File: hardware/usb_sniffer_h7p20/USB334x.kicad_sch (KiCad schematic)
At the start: 16 parts, among them J2 USB_C_Receptacle_USB2.0_16P, J3 USB_A, U10 CH132C, U2 LM2903A-VR, U3 LM2903A-VR, U4 LM2903A-VR

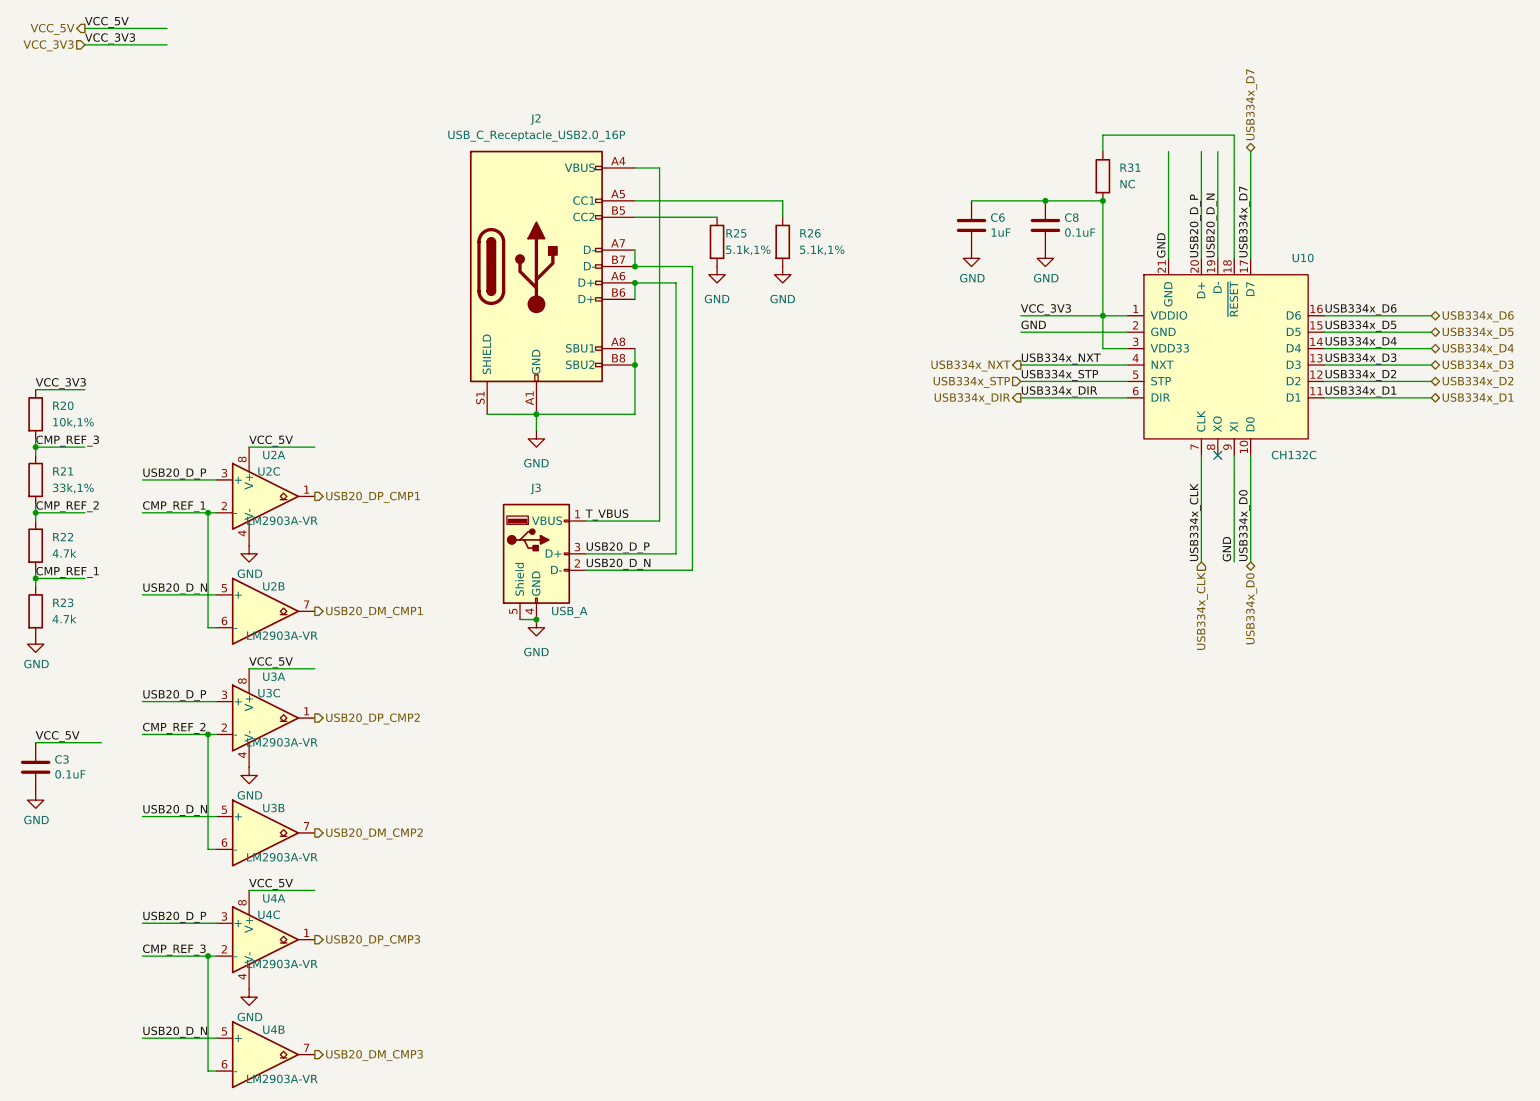
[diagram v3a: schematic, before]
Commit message: [usb_sniffer_h7p20] CH132C测试无数据，回退USB3343
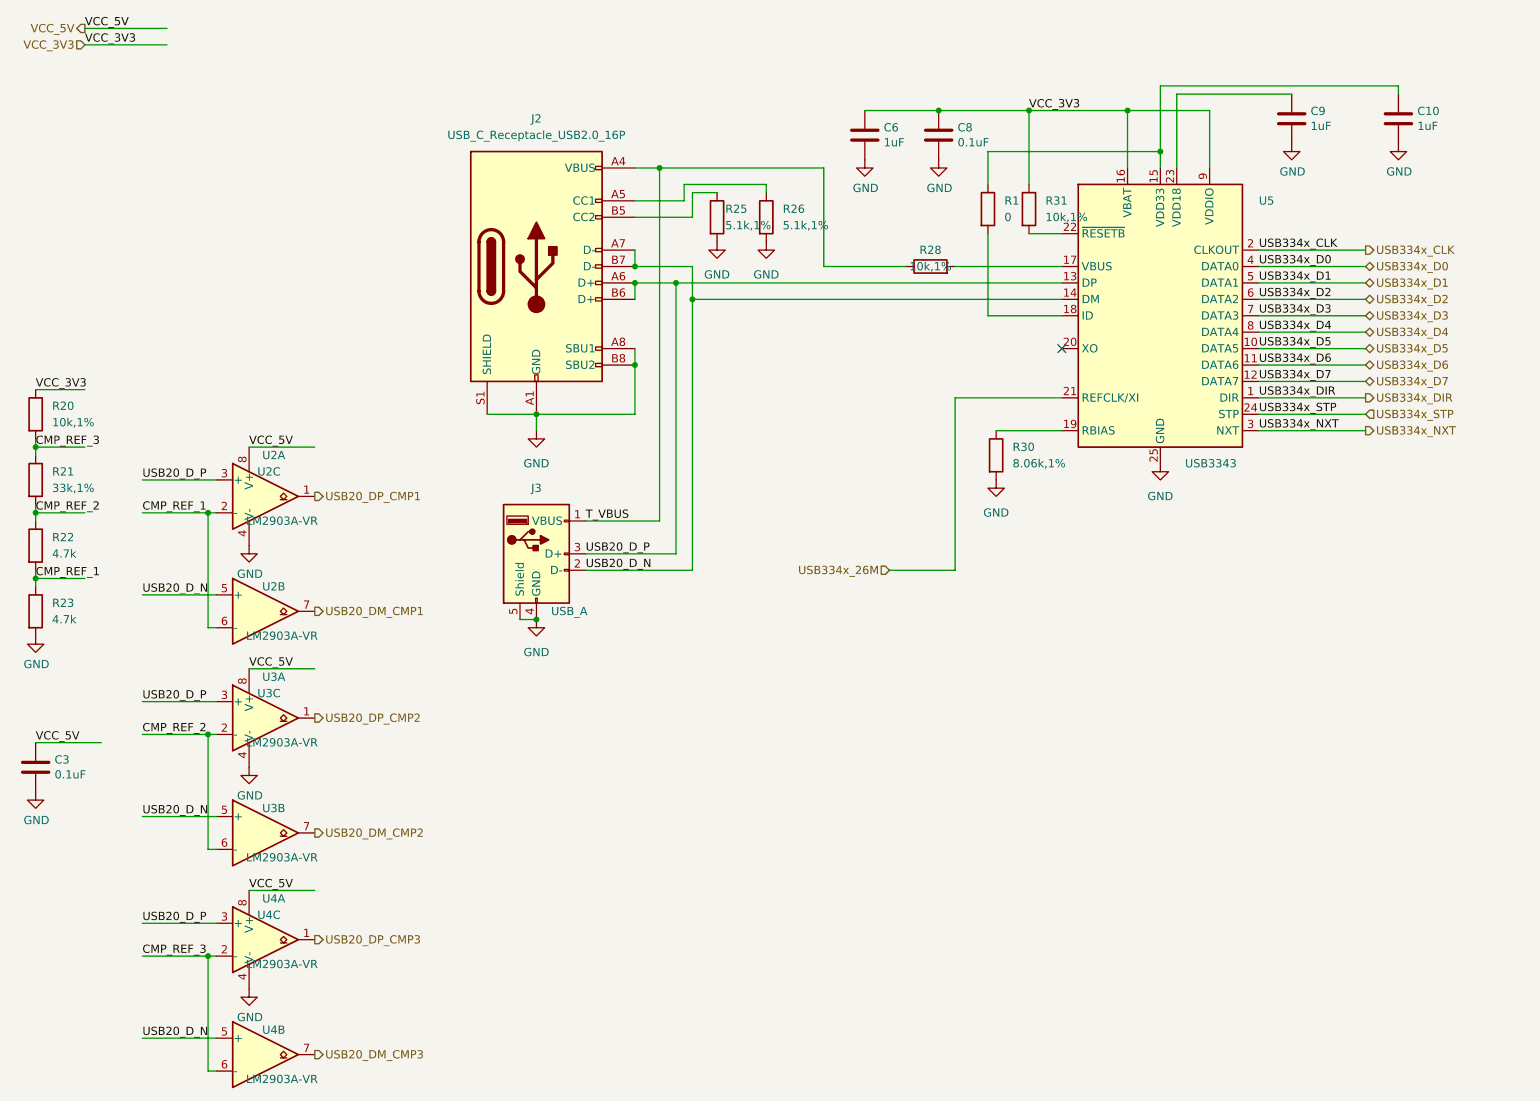
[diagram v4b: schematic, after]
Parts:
- removed U10: CH132C, vllogic:QFN20C_2x2, symbol vllogic_chip:CH132C
- added C10, C9: 1uF, Capacitor_SMD:C_0402_1005Metric, symbol Device:C
- added R1: 0, Resistor_SMD:R_0402_1005Metric, symbol Device:R
- added R28: 10k,1%, Resistor_SMD:R_0402_1005Metric, symbol Device:R
- added R30: 8.06k,1%, Resistor_SMD:R_0402_1005Metric, symbol Device:R
- added U5: USB3343, vllogic:QFN-24-1EP_4x4mm_P0.5mm_EP2.6x2.6mm, symbol Interface_USB:USB3343
- R31: value NC -> 10k,1%
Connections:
- net GND: now also C10.1, C9.1, R30.2, U5.25 (GND)
- net T_VBUS: now also R28.1
- net USB20_D_N: now also U5.14 (DM)
- net USB20_D_P: now also U5.13 (DP)
- net USB334x_CLK: now also U5.2 (CLKOUT)
- net USB334x_D0: now also U5.4 (DATA0)
- net USB334x_D1: now also U5.5 (DATA1)
- net USB334x_D2: now also U5.6 (DATA2)
- net USB334x_D3: now also U5.7 (DATA3)
- net USB334x_D4: now also U5.8 (DATA4)
- net USB334x_D5: now also U5.10 (DATA5)
- net USB334x_D6: now also U5.11 (DATA6)
- net USB334x_D7: now also U5.12 (DATA7)
- net USB334x_DIR: now also U5.1 (DIR)
- net USB334x_NXT: now also U5.3 (NXT)
- net USB334x_STP: now also U5.24 (STP)
- net VCC_3V3: now also R31.1, U5.16 (VBAT), U5.9 (VDDIO); no longer R31.2
- new net: R31.2, U5.22 (~{RESETB})
- new net: R30.1, U5.19 (RBIAS)
- new net: C10.2, R1.1, U5.15 (VDD33)
- new net: R28.2, U5.17 (VBUS)
- new net: R1.2, U5.18 (ID)
- new net: C9.2, U5.23 (VDD18)
- new net USB334x_26M: U5.21 (REFCLK/XI)
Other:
- moved on the sheet: C6, C8, R25, R26, R31

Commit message: [usb_sniffer_h7p20] 换GSV332-MR，待测试
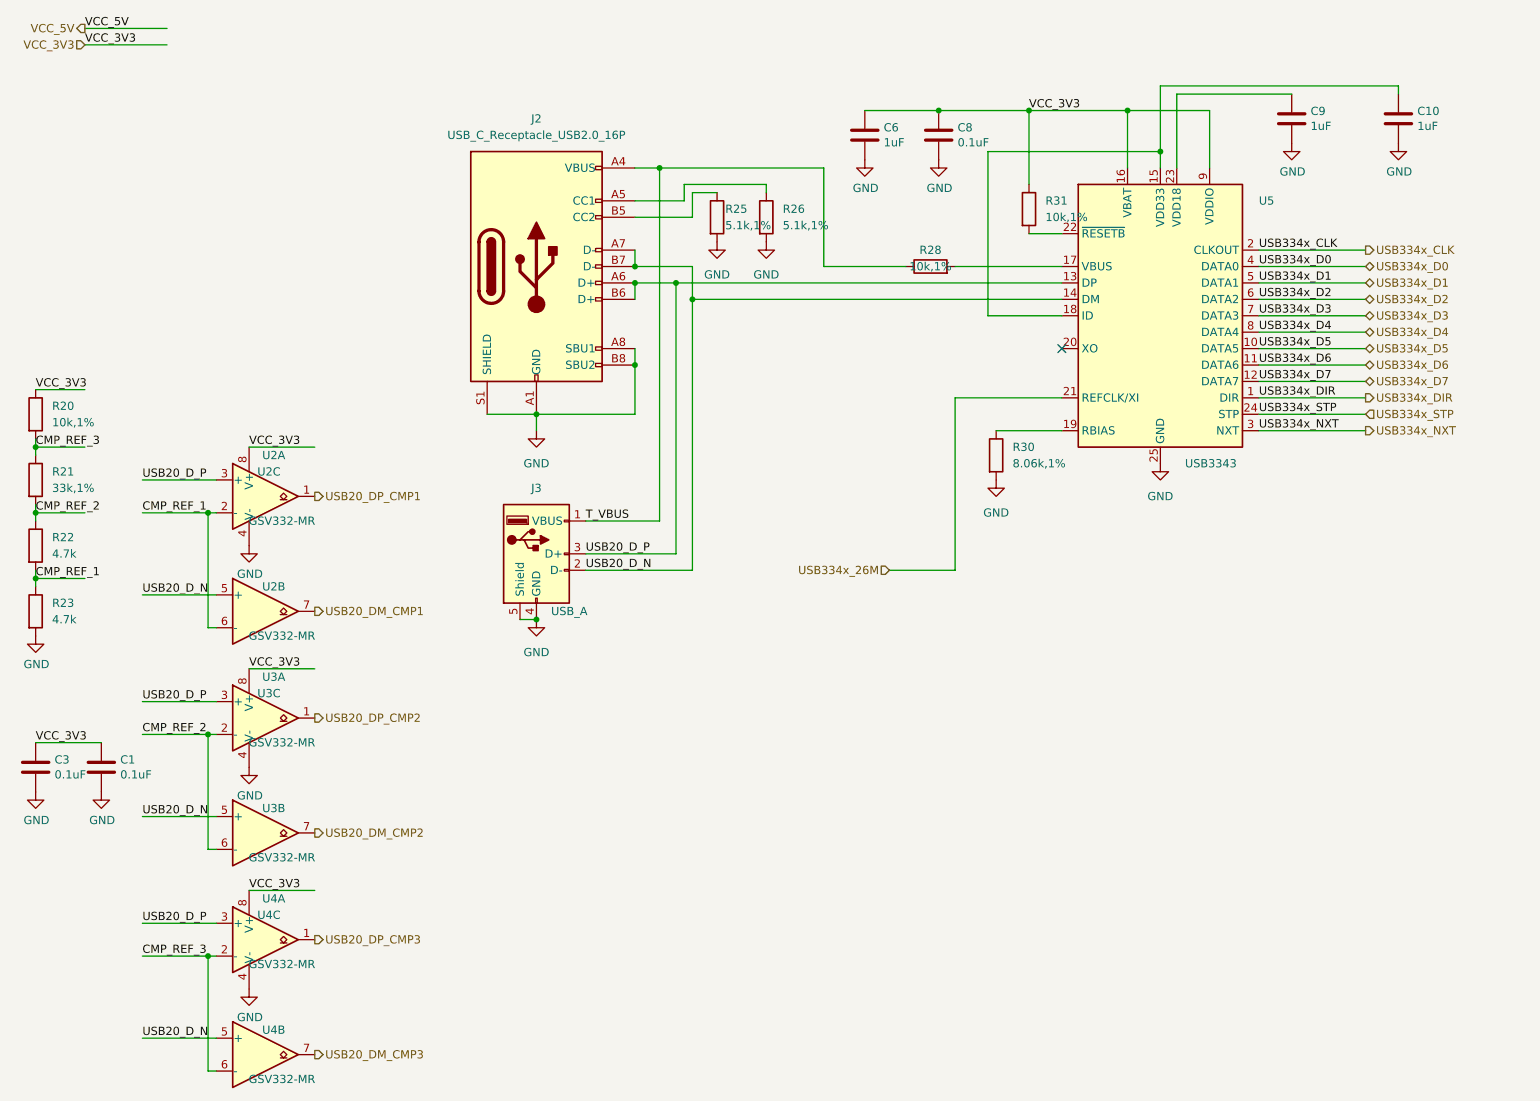
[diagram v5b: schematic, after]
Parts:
- removed R1: 0, Resistor_SMD:R_0402_1005Metric, symbol Device:R
- added C1: 0.1uF, Capacitor_SMD:C_0402_1005Metric, symbol Device:C
- U2, U3, U4: value LM2903A-VR -> GSV332-MR
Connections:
- net GND: now also C1.1
- net VCC_3V3: now also C3.2, U2.8 (V+), U3.8 (V+), U4.8 (V+), C1.2
- net VCC_5V: no longer C3.2, U2.8 (V+), U3.8 (V+), U4.8 (V+)
- net at C10.2, U5.15 (VDD33): now also U5.18 (ID)
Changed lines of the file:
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@@
 	(wire
 		(pts
-			(xy 171.45 50.8) (xy 171.45 55.88)
-		)
-		(stroke
-			(width 0)
-			(type default)
-		)
-	)
-	(wire
-		(pts
 			(xy 213.36 81.28) (xy 229.87 81.28)
 		)
@@
 	(wire
 		(pts
-			(xy 171.45 63.5) (xy 171.45 76.2)
+			(xy 171.45 50.8) (xy 171.45 76.2)
 		)
 		(stroke
@@
 		)
 	)
-	(label "VCC_5V"
-		(at 57.15 130.81 0)
+	(label "VCC_3V3"
+		(at 24.13 87.63 0)
 		(effects
 			(font
@@
 		)
 	)
-	(label "VCC_3V3"
-		(at 24.13 87.63 0)
+	(label "USB334x_NXT"
+		(at 213.36 93.98 0)
 		(effects
 			(font
@@
 		)
 	)
-	(label "USB334x_NXT"
-		(at 213.36 93.98 0)
+	(label "VCC_3V3"
+		(at 24.13 142.24 0)
 		(effects
 			(font
@@
 		)
 	)
-	(label "VCC_5V"
-		(at 57.15 96.52 0)
-		(effects
-			(font
-				(size 1.27 1.27)
-			)
-			(justify left bottom)
-		)
-	)
-	(label "VCC_5V"
-		(at 57.15 165.1 0)
-		(effects
-			(font
-				(size 1.27 1.27)
-			)
-			(justify left bottom)
-		)
-	)
 	(label "CMP_REF_3"
 		(at 40.64 175.26 0)
@@
 		)
 	)
-	(label "VCC_5V"
-		(at 24.13 142.24 0)
+	(label "USB334x_D4"
+		(at 213.36 78.74 0)
 		(effects
 			(font
@@
 		)
 	)
-	(label "USB334x_D4"
-		(at 213.36 78.74 0)
+	(label "CMP_REF_3"
+		(at 24.13 96.52 0)
 		(effects
 			(font
@@
 		)
 	)
-	(label "CMP_REF_3"
-		(at 24.13 96.52 0)
+	(label "VCC_3V3"
+		(at 57.15 165.1 0)
 		(effects
 			(font
@@
 		)
 	)
+	(label "VCC_3V3"
+		(at 57.15 130.81 0)
+		(effects
+			(font
+				(size 1.27 1.27)
+			)
+			(justify left bottom)
+		)
+	)
 	(label "USB334x_D6"
 		(at 213.36 83.82 0)
@@
 		)
 	)
+	(label "VCC_3V3"
+		(at 57.15 96.52 0)
+		(effects
+			(font
+				(size 1.27 1.27)
+			)
+			(justify left bottom)
+		)
+	)
 	(label "USB334x_D3"
 		(at 213.36 76.2 0)
@@
 			)
 		)
-		(property "Value" "LM2903A-VR"
+		(property "Value" "GSV332-MR"
 			(at 58.42 142.24 0)
 			(effects
@@
 			)
 		)
-		(property "Value" "LM2903A-VR"
+		(property "Value" "GSV332-MR"
 			(at 62.23 142.24 0)
 			(effects
@@
 			)
 		)
-		(property "Value" "LM2903A-VR"
+		(property "Value" "GSV332-MR"
 			(at 62.23 160.02 0)
 			(effects
@@
 	)
 	(symbol
+		(lib_id "power:GND")
+		(at 34.29 149.86 0)
+		(unit 1)
+		(exclude_from_sim no)
+		(in_bom yes)
+		(on_board yes)
+		(dnp no)
+		(property "Reference" "#PWR01"
+			(at 34.29 156.21 0)
+			(effects
+				(font
+					(size 1.27 1.27)
+				)
+				(hide yes)
+			)
+		)
+		(property "Value" "GND"
+			(at 34.417 154.2542 0)
+			(effects
+				(font
+					(size 1.27 1.27)
+				)
+			)
+		)
+		(property "Footprint" ""
+			(at 34.29 149.86 0)
+			(effects
+				(font
+					(size 1.27 1.27)
+				)
+				(hide yes)
+			)
+		)
+		(property "Datasheet" ""
+			(at 34.29 149.86 0)
+			(effects
+				(font
+					(size 1.27 1.27)
+				)
+				(hide yes)
+			)
+		)
+		(property "Description" ""
+			(at 34.29 149.86 0)
+			(effects
+				(font
+					(size 1.27 1.27)
+				)
+			)
+		)
+		(pin "1"
+		)
+		(instances
+			(project "usb_sniffer_h7p20"
+				(path "/5a8287a8-9f7a-4e60-a3bf-19c1227b20fe/f5b7f82e-a1df-40b6-9f59-134d2c724739"
+					(reference "#PWR01")
+					(unit 1)
+				)
+			)
+		)
+	)
+	(symbol
 		(lib_id "Connector:USB_A")
 		(at 101.6 113.03 0)
@@
 			)
 		)
-		(property "Datasheet" " ~"
+		(property "Datasheet" "~"
 			(at 105.41 114.3 0)
 			(effects
@@
 			)
 		)
-		(property "Value" "LM2903A-VR"
+		(property "Value" "GSV332-MR"
 			(at 62.23 107.95 0)
 			(effects
@@
 			)
 		)
-		(property "Value" "LM2903A-VR"
+		(property "Value" "GSV332-MR"
 			(at 62.23 125.73 0)
 			(effects
@@
 	)
 	(symbol
+		(lib_id "Device:C")
+		(at 34.29 146.05 180)
+		(unit 1)
+		(exclude_from_sim no)
+		(in_bom yes)
+		(on_board yes)
+		(dnp no)
+		(property "Reference" "C1"
+			(at 37.211 144.8816 0)
+			(effects
+				(font
+					(size 1.27 1.27)
+				)
+				(justify right)
+			)
+		)
+		(property "Value" "0.1uF"
+			(at 37.211 147.193 0)
+			(effects
+				(font
+					(size 1.27 1.27)
+				)
+				(justify right)
+			)
+		)
+		(property "Footprint" "Capacitor_SMD:C_0402_1005Metric"
+			(at 33.3248 142.24 0)
+			(effects
+				(font
+					(size 1.27 1.27)
+				)
+				(hide yes)
+			)
+		)
+		(property "Datasheet" "~"
+			(at 34.29 146.05 0)
+			(effects
+				(font
+					(size 1.27 1.27)
+				)
+				(hide yes)
+			)
+		)
+		(property "Description" ""
+			(at 34.29 146.05 0)
+			(effects
+				(font
+					(size 1.27 1.27)
+				)
+			)
+		)
+		(pin "1"
+		)
+		(pin "2"
+		)
+		(instances
+			(project "usb_sniffer_h7p20"
+				(path "/5a8287a8-9f7a-4e60-a3bf-19c1227b20fe/f5b7f82e-a1df-40b6-9f59-134d2c724739"
+					(reference "C1")
+					(unit 1)
+				)
+			)
+		)
+	)
+	(symbol
 		(lib_id "Comparator:LM2903")
 		(at 59.69 104.14 0)
@@
 			)
 		)
-		(property "Value" "LM2903A-VR"
+		(property "Value" "GSV332-MR"
 			(at 58.42 107.95 0)
 			(effects
@@
 			)
 		)
-		(property "Value" "LM2903A-VR"
+		(property "Value" "GSV332-MR"
 			(at 62.23 176.53 0)
 			(effects
@@
 	)
 	(symbol
-		(lib_id "Device:R")
-		(at 171.45 59.69 0)
-		(unit 1)
-		(exclude_from_sim no)
-		(in_bom yes)
-		(on_board yes)
-		(dnp no)
-		(fields_autoplaced yes)
-		(property "Reference" "R1"
-			(at 173.99 58.42 0)
-			(effects
-				(font
-					(size 1.27 1.27)
-				)
-				(justify left)
-			)
-		)
-		(property "Value" "0"
-			(at 173.99 60.96 0)
-			(effects
-				(font
-					(size 1.27 1.27)
-				)
-				(justify left)
-			)
-		)
-		(property "Footprint" "Resistor_SMD:R_0402_1005Metric"
-			(at 169.672 59.69 90)
-			(effects
-				(font
-					(size 1.27 1.27)
-				)
-				(hide yes)
-			)
-		)
-		(property "Datasheet" "~"
-			(at 171.45 59.69 0)
-			(effects
-				(font
-					(size 1.27 1.27)
-				)
-				(hide yes)
-			)
-		)
-		(property "Description" ""
-			(at 171.45 59.69 0)
-			(effects
-				(font
-					(size 1.27 1.27)
-				)
-			)
-		)
-		(pin "2"
-		)
-		(pin "1"
-		)
-		(instances
-			(project "usb_sniffer_h7p20"
-				(path "/5a8287a8-9f7a-4e60-a3bf-19c1227b20fe/f5b7f82e-a1df-40b6-9f59-134d2c724739"
-					(reference "R1")
-					(unit 1)
-				)
-			)
-		)
-	)
-	(symbol
 		(lib_id "Comparator:LM2903")
 		(at 59.69 190.5 0)
@@
 			)
 		)
-		(property "Value" "LM2903A-VR"
+		(property "Value" "GSV332-MR"
 			(at 62.23 194.31 0)
 			(effects
@@
 			)
 		)
-		(property "Value" "LM2903A-VR"
+		(property "Value" "GSV332-MR"
 			(at 58.42 176.53 0)
 			(effects
